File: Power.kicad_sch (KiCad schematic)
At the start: 10 parts, among them J901 Barrel_Jack_MountingPin, J902 Barrel_Jack_MountingPin, U901 AZ1117-3.3

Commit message: [FIX] changed type of barrel jack to correct one
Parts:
- J901, J902: footprint Connector_BarrelJack:BarrelJack_Wuerth_6941xx301002 -> Connector_BarrelJack:BarrelJack_Horizontal
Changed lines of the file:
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@@
     (property "Reference" "J902" (id 0) (at 60.96 95.25 0))
     (property "Value" "Barrel_Jack_MountingPin" (id 1) (at 60.96 97.79 0))
-    (property "Footprint" "Connector_BarrelJack:BarrelJack_Wuerth_6941xx301002" (id 2) (at 62.23 105.156 0)
+    (property "Footprint" "Connector_BarrelJack:BarrelJack_Horizontal" (id 2) (at 62.23 105.156 0)
       (effects (font (size 1.27 1.27)) hide)
     )
@@
     (property "Reference" "J901" (id 0) (at 60.96 74.295 0))
     (property "Value" "Barrel_Jack_MountingPin" (id 1) (at 60.96 76.835 0))
-    (property "Footprint" "Connector_BarrelJack:BarrelJack_Wuerth_6941xx301002" (id 2) (at 62.23 84.201 0)
+    (property "Footprint" "Connector_BarrelJack:BarrelJack_Horizontal" (id 2) (at 62.23 84.201 0)
       (effects (font (size 1.27 1.27)) hide)
     )

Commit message: update plików
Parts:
- removed C901: 10uF, Capacitor_THT:CP_Radial_D5.0mm_P2.00mm, symbol Device:C_Polarized
- added F902: Fuse, Fuse:Fuse_Bourns_MF-RHT1000, symbol Device:Fuse
- added J901, J904: ARK 5mm, TerminalBlock_Philmore:TerminalBlock_Philmore_TB132_1x02_P5.00mm_Horizontal, symbol Connector:Screw_Terminal_01x02
- added J905, J906: JST 2.54mm, Connector_JST:JST_XH_B2B-XH-A_1x02_P2.50mm_Vertical, symbol Connector:Conn_01x02_Male
- renumbered C902 to C901, C903 to C902, C904 to C903, J901 to J902, J902 to J903
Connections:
- net 5V: now also J906.1 (Pin_1)
- net GND: now also J901.1 (Pin_1), J905.2 (Pin_2), J906.2 (Pin_2)
- net VIN_CONN: now also F901.1, J901.2 (Pin_2); no longer D901.1 (K)
- net VIN_CONN2: now also F902.2; no longer D901.3 (K)
- net VIN_FUSE: now also J904.2 (Pin_2); no longer F901.1
- net V_IN: now also J904.1 (Pin_1), J905.1 (Pin_1); no longer F901.2
- new net: D901.1 (K), F901.2
- new net: D901.3 (K), F902.1
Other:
- company: (none) -> Szymon Przybył
- title: (none) -> Power supplies
- moved on the sheet: D901

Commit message: schematic update after meeting
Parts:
- removed J906: JST 2.54mm, Connector_JST:JST_XH_B2B-XH-A_1x02_P2.50mm_Vertical, symbol Connector:Conn_01x02_Male
- added J905: JST 2.54mm, Connector_JST:JST_XH_B2B-XH-A_1x02_P2.50mm_Vertical, symbol Connector:Conn_01x02_Male
- added J907: JST 2.56mm, Connector_JST:JST_XH_B4B-XH-A_1x04_P2.50mm_Vertical, symbol Connector:Conn_01x04_Male
- renumbered J905 to J906
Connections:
- net 5V: now also J907.1 (Pin_1), J907.2 (Pin_2)
- net GND: now also J905.2 (Pin_2), J907.3 (Pin_3), J907.4 (Pin_4)
- net V_IN: now also J905.1 (Pin_1)

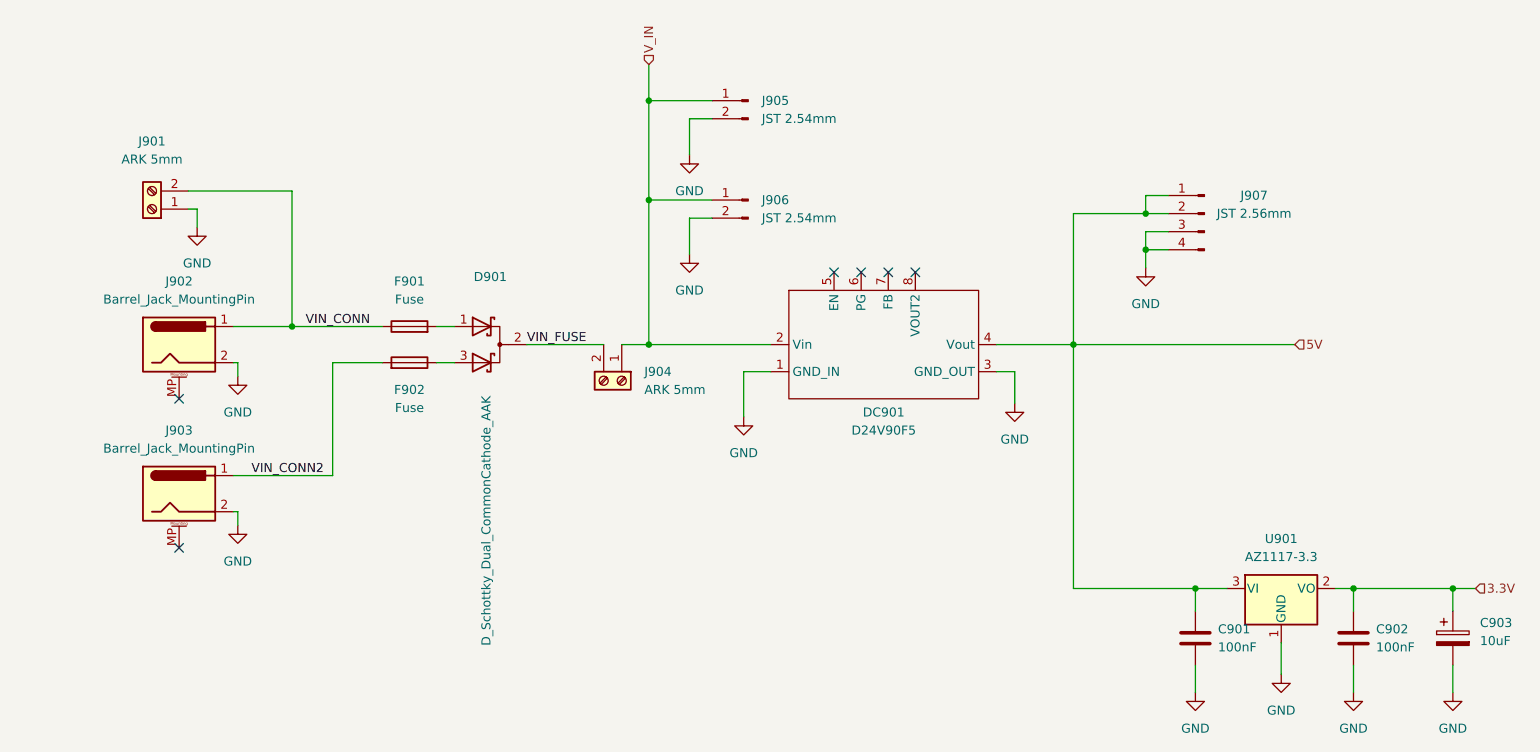
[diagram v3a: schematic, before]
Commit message: layout update moved power section to the bottom of the board, ibom generated, changed footprint for switches
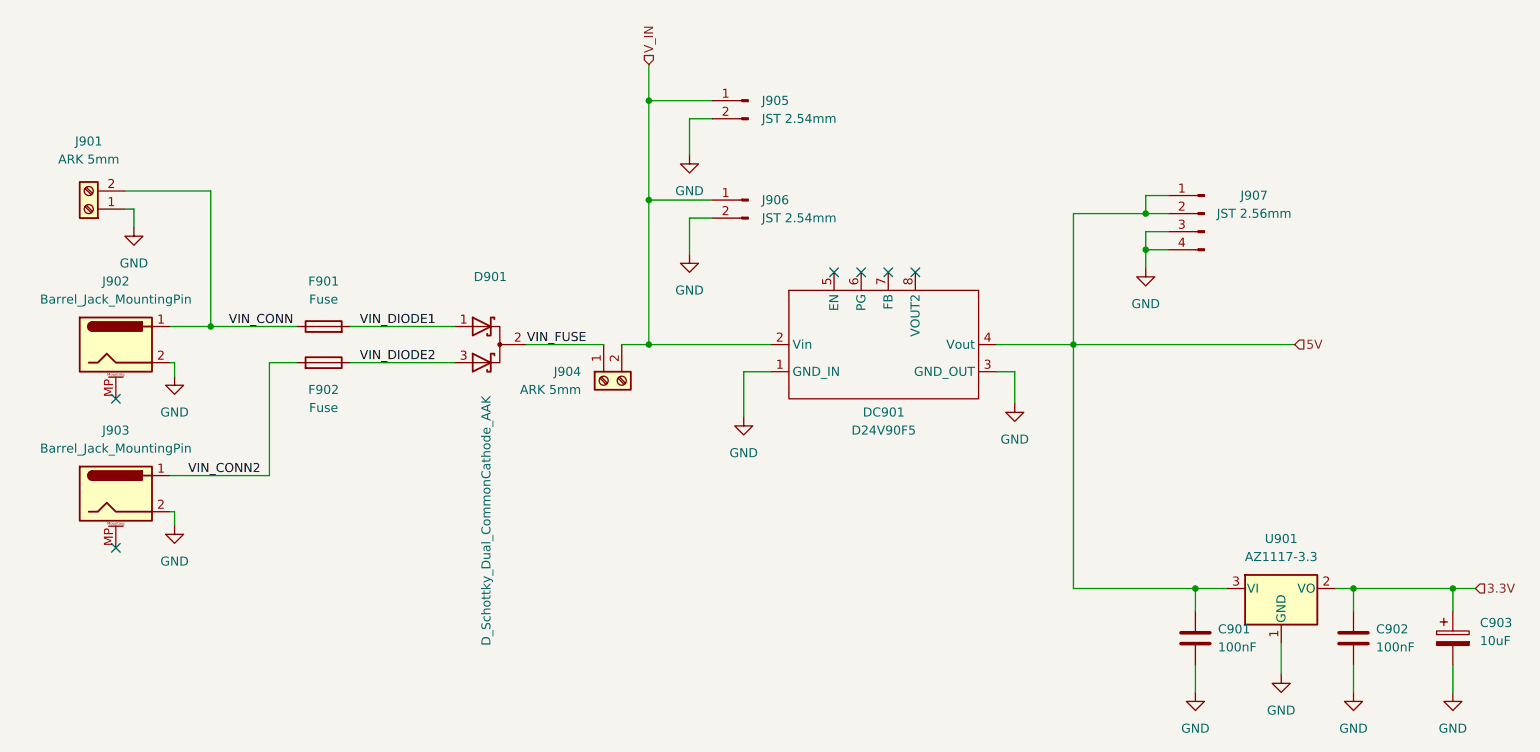
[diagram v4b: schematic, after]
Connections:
- net VIN_FUSE: now also J904.1 (Pin_1); no longer J904.2 (Pin_2)
- net V_IN: now also J904.2 (Pin_2); no longer J904.1 (Pin_1)
- net VIN_DIODE1: now reaches D901.1 (K), F901.2
- net VIN_DIODE2: now reaches D901.3 (K), F902.1
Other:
- moved on the sheet: F901, F902, J901, J902, J903, J904
